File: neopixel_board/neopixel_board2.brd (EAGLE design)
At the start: 160 x 100 mm, 44 parts, among them J1 SSW-102-02-T-S-RA, J2 SSW-102-02-T-S-RA, J3 SSW-102-02-T-S-RA, J4 SSW-102-02-T-S-RA, U2 MIC5219, U3 ATMEGA32U4, Y1 16MHz

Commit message: board WIP traces started
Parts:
- added LD4, LD5, LD6: GREEN, SparkFun-LED:LED-0603
- added R10, R12, R9: 1kΩ, SparkFun:0603-RES
- moved R5 144.8 mm to (3.81, 3.81), turned to 90 degrees
- moved R4 134.9 mm to (12.7, 26.7)
- moved R7 134.7 mm to (7.62, 3.81), turned to 90 degrees
- moved D1 128.4 mm to (11.4, 3.81), turned to 90 degrees
- moved C13 120.9 mm to (38.1, 29.2)
- moved C19 113.7 mm to (38.1, 33.0)
- moved R2 112.1 mm to (49.5, 19.1), turned to 90 degrees
- moved R8 105.0 mm to (58.4, 7.62), turned to 90 degrees
- moved R3 104.0 mm to (34.3, 53.3), turned to 90 degrees
- moved C6 100.7 mm to (53.3, 7.62), turned to 90 degrees
- moved R6 100.6 mm to (49.5, 7.62), turned to 270 degrees
- moved C18 99.3 mm to (49.5, 30.5)
- moved C5 96.6 mm to (54.6, 22.9), turned to 90 degrees
- moved U2 94.8 mm to (44.5, 30.5)
- moved LD1 89.9 mm to (49.5, 2.54)
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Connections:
- new net N$14: LD4.A, R12.1
- new net N$15: LD5.A, R10.1
- new net N$16: LD6.A, R9.1
- net GND: now also LD4.C, LD5.C, LD6.C
- net N$10: now also R9.2
- net N$11: now also R10.2
- net N$12: now also R12.2
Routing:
- net GND: track 0.00 -> 338.9 mm, vias 0 -> 1
- net VCC1_3.3V: track 0.00 -> 130.7 mm, vias 0 -> 7
- net RAW: track 0.00 -> 93.3 mm
- net VCC_5V: track 0.00 -> 58.0 mm
- net ETH_RST: track 0.00 -> 56.8 mm, vias 0 -> 3
- net MCU_RST: track 0.00 -> 56.4 mm, vias 0 -> 3
- net D+: track 0.00 -> 41.7 mm
- net N$4: track 0.00 -> 34.1 mm, vias 0 -> 2
- net TXLED: track 0.00 -> 24.0 mm, vias 0 -> 2
- net ETH_SCNN: track 0.00 -> 22.9 mm, vias 0 -> 2
- net NEOPIXEL_0: track 0.00 -> 20.6 mm, vias 0 -> 2
- net N$3: track 0.00 -> 18.0 mm
- net N$12: track 0.00 -> 17.2 mm
- net N$11: track 0.00 -> 17.1 mm
- net N$10: track 0.00 -> 17.1 mm
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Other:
- board size 160 x 100 mm -> 60.9 x 75.9 mm

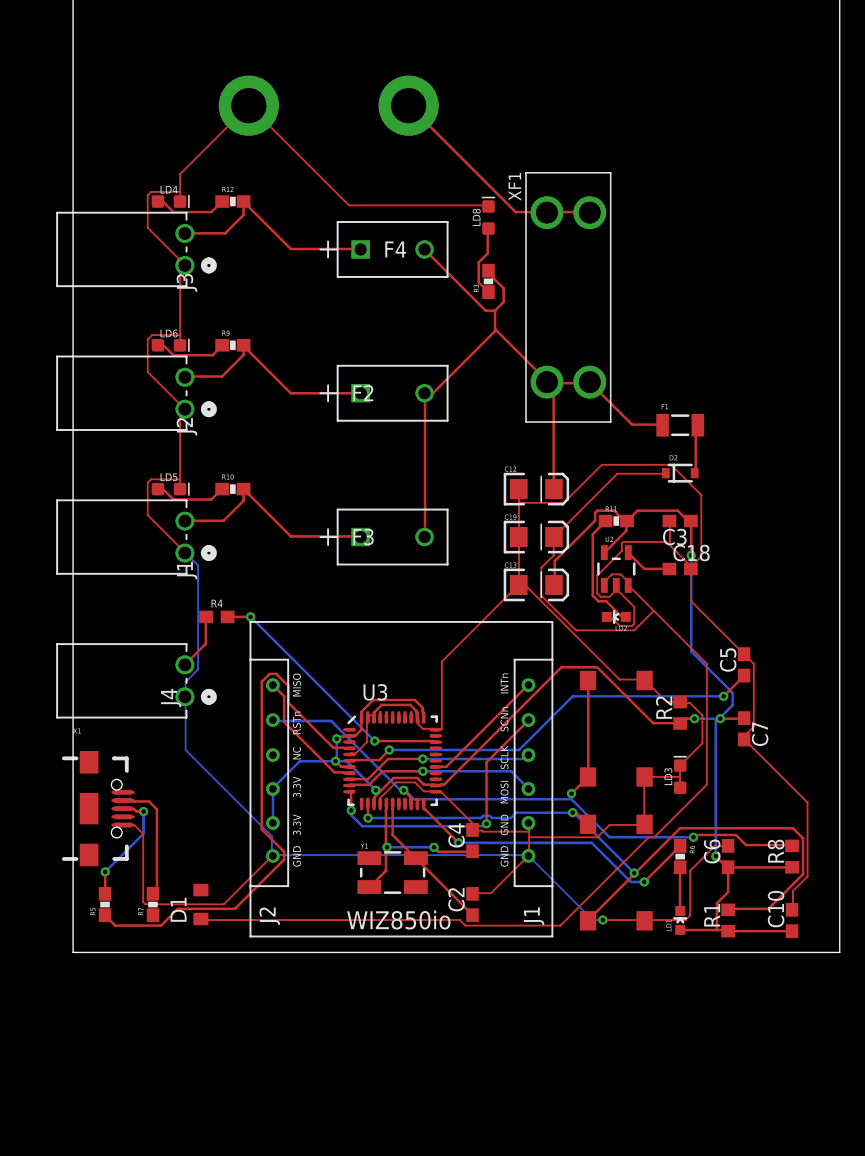
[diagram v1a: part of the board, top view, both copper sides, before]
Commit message: Schematic WIP
added new USB programmer, replaced fuse, ripup of autoroute
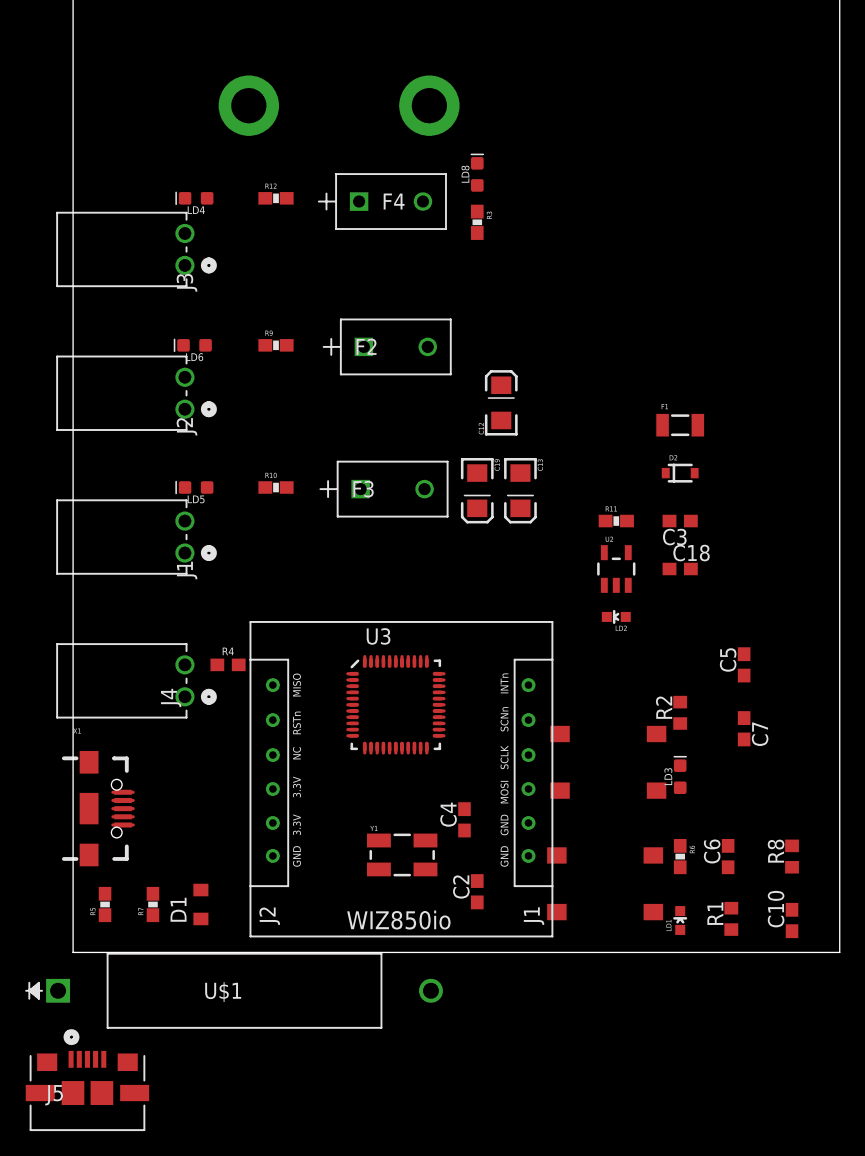
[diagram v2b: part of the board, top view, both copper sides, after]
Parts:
- removed XF1: 13A, RoboJackets-Fuses:3557-2
- added J5: 1981584-1, neopixel_board:CONN5_1981584-1
- added U$1: NEW_5STP, neopixel_board:5SP_AXIAL
- moved C13 7.60 mm to (36.8, 36.7), turned to 270 degrees
- moved C12 7.41 mm to (35.3, 43.7), turned to 90 degrees
- moved C19 5.97 mm to (33.4, 36.7), turned to 270 degrees
- moved R3 4.78 mm to (33.4, 58.0), turned to 270 degrees
- moved U3 4.45 mm to (26.9, 19.7)
- moved R4 3.91 mm to (13.6, 22.9)
- moved F4 3.81 mm to (29.1, 59.7)
- moved F3 3.81 mm to (29.2, 36.8)
- moved F2 3.69 mm to (29.5, 48.1)
- moved LD8 3.54 mm to (33.4, 61.8)
- moved R12 3.44 mm to (17.4, 59.9)
- moved R10 3.43 mm to (17.4, 37.0)
- moved R9 3.43 mm to (17.4, 48.3)
- moved PB2 2.74 mm to (43.8, 15.1), turned to 180 degrees
- moved LD4 2.17 mm to (11.0, 59.9), turned to 180 degrees
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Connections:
- net N$3: no longer XF1.1, XF1.2
- net VCC_5V: no longer XF1.3, XF1.4
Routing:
- net GND: track 338.9 -> 0.00 mm, vias 1 -> 0
- net VCC1_3.3V: track 130.7 -> 0.00 mm, vias 7 -> 0
- net RAW: track 93.3 -> 0.00 mm
- net VCC_5V: track 58.0 -> 0.00 mm
- net ETH_RST: track 56.8 -> 0.00 mm, vias 3 -> 0
- net MCU_RST: track 56.4 -> 0.00 mm, vias 3 -> 0
- net D+: track 41.7 -> 0.00 mm
- net N$4: track 34.1 -> 0.00 mm, vias 2 -> 0
- net TXLED: track 24.0 -> 0.00 mm, vias 2 -> 0
- net ETH_SCNN: track 22.9 -> 0.00 mm, vias 2 -> 0
- net NEOPIXEL_0: track 20.6 -> 0.00 mm, vias 2 -> 0
- net N$3: track 18.0 -> 0.00 mm
- net N$12: track 17.2 -> 0.00 mm
- net N$11: track 17.1 -> 0.00 mm
- net N$10: track 17.1 -> 0.00 mm
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
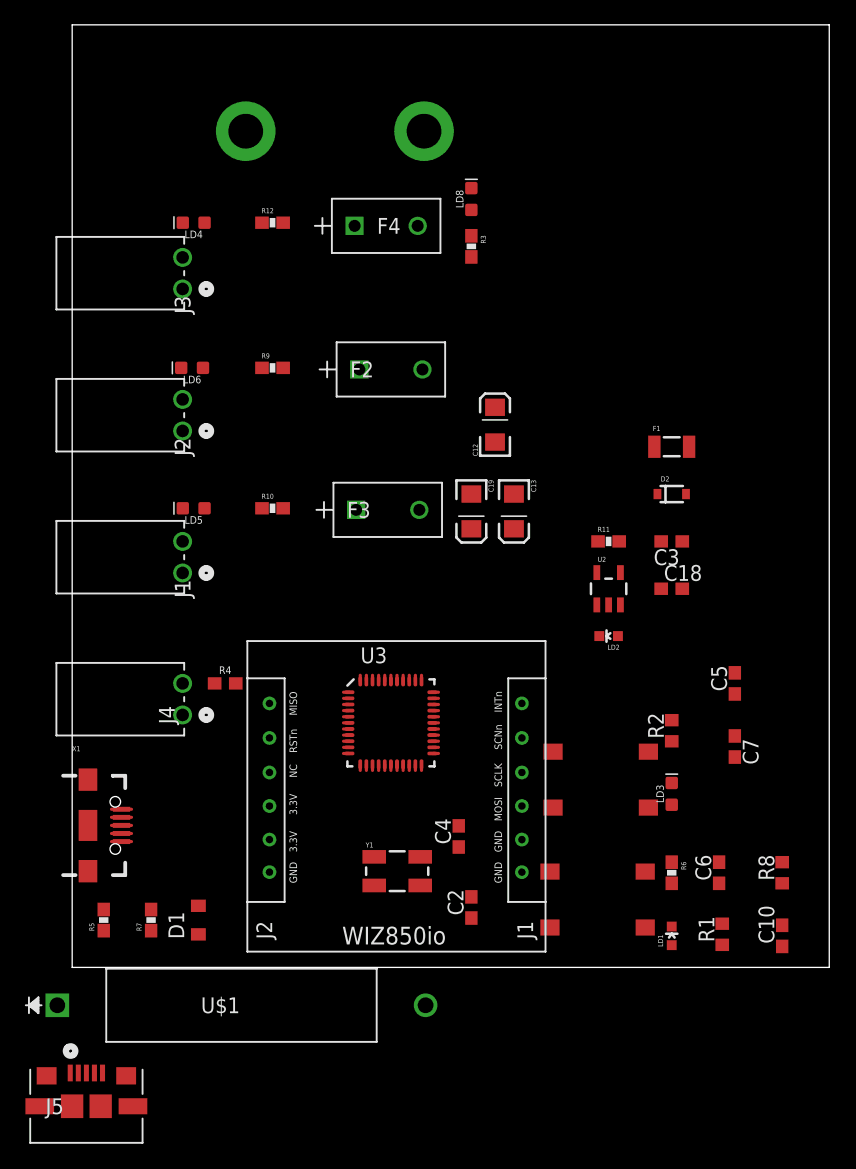
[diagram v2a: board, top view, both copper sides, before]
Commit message: Board, Schematic, Library WIP
Updated MCU, USB library layout of board completed, need to route
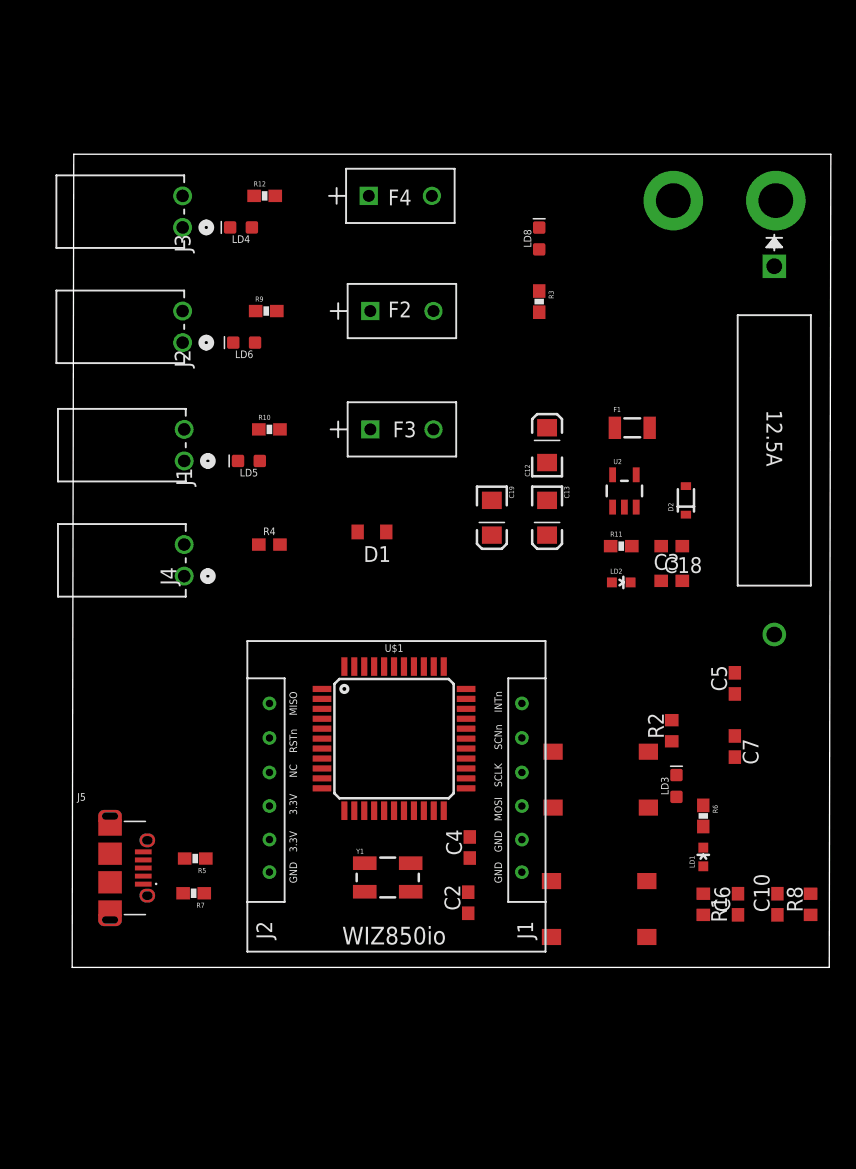
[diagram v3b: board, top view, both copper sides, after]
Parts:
- removed U3: ATMEGA32U4, Testing:QFN-44-NOPAD_1:1-OUTFAKES
- removed X1: (no value), Testing:USB-AB-MICRO-SMD-V03-IN&OUT
- added 12.5A: NEW_5STP, neopixel_board:5SP_AXIAL
- J5: value 1981584-1 -> 47589-0001; device neopixel_board:CONN5_1981584-1 -> 47589-0001:MOLEX_47589-0001
- U$1: value NEW_5STP -> 32U4; device neopixel_board:5SP_AXIAL -> SparkFun-IC-Microcontroller:TQFP44
- moved GND_TERMINAL 34.9 mm to (49.7, 61.7)
- moved D1 34.2 mm to (25.4, 35.1), turned to 180 degrees
- moved 5VSOURCE 28.9 mm to (57.9, 61.7)
- moved U$1 21.6 mm to (27.2, 18.4)
- moved J5 19.3 mm to (4.32, 8.00)
- moved R4 11.7 mm to (17.1, 34.0)
- moved J4 11.2 mm to (10.3, 32.8)
- moved J1 9.02 mm to (10.3, 42.0)
- moved R5 8.88 mm to (11.2, 8.76), turned to 180 degrees
- moved U2 7.98 mm to (45.7, 38.4)
- moved J2 7.11 mm to (10.2, 51.6)
- moved R3 7.04 mm to (38.9, 53.6)
- moved LD1 6.84 mm to (52.1, 8.89)
- moved F3 6.58 mm to (30.4, 43.3)
- moved R10 6.36 mm to (17.1, 43.3)
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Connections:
- removed net UVCC: D1.A, X1.VBUS1
- new net N$17: D1.A, J5.1
- new net N$18: LD3.A, R2.2
- net D+: now also U$1.4; no longer U3.4
- net D-: now also U$1.3; no longer U3.3
- net ETH_INT: now also U$1.27; no longer U3.27
- net ETH_MISO: now also U$1.8; no longer U3.8
- net ETH_MOSI: now also U$1.10; no longer U3.10
- net ETH_RST: now also U$1.20; no longer U3.20
- net ETH_SCK: now also U$1.9; no longer U3.9
- net ETH_SCNN: now also U$1.11; no longer U3.11
- net GND: now also J5.5, J5.P$1, J5.P$2, J5.P$3, J5.P$4, J5.P$5, J5.P$6, U$1.15, U$1.23, U$1.33, U$1.35, U$1.42, U$1.43, U$1.5; no longer LD3.A, R2.2, U3.15, U3.23, U3.33, U3.35, U3.42, U3.43, U3.5, X1.GND1
- net MCU_RST: now also U$1.13; no longer U3.13
- net N$1: now also U$1.16; no longer U3.16
- net N$2: now also U$1.17; no longer U3.17
- net N$3: now also 12.5A.1
- net N$4: now also U$1.6; no longer U3.6
- net N$6: now also J5.2; no longer X1.D-1
- net N$8: now also J5.3; no longer X1.D+1
- net NEOPIXEL_0: now also U$1.31; no longer U3.31
- net TXLED: now also U$1.22; no longer U3.22
- net VCC1_3.3V: now also U$1.14, U$1.2, U$1.24, U$1.34, U$1.44, U$1.7; no longer U3.14, U3.2, U3.24, U3.34, U3.44, U3.7
- net VCC_5V: now also 12.5A.2
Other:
- board size 60.9 x 75.9 mm -> 61.1 x 65.5 mm

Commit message: Board WIP
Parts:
- 12.5A: value NEW_5STP -> (none); device neopixel_board:5SP_AXIAL -> neopixel_board:3557-2
- F2, F3, F4: value RST_4-BULK -> (none); device neopixel_board:RST -> neopixel_board:3557-2
- moved 12.5A 26.8 mm to (49.9, 52.5)
- moved D1 21.1 mm to (43.9, 24.9)
- moved C12 18.2 mm to (57.4, 45.2)
- moved F1 12.9 mm to (57.1, 36.4)
- moved GND_TERMINAL 11.6 mm to (57.4, 53.1)
- moved LD5 9.78 mm to (5.71, 40.9)
- moved LD6 9.41 mm to (5.71, 50.7)
- moved R4 9.23 mm to (9.53, 28.8)
- moved LD4 9.20 mm to (5.71, 60.6)
- moved R10 7.99 mm to (9.53, 40.9)
- moved J4 7.88 mm to (9.91, 24.9)
- moved R9 7.68 mm to (9.53, 50.7)
- moved R12 7.40 mm to (9.53, 60.6)
- moved C13 5.51 mm to (40.3, 30.7)
- moved C19 5.36 mm to (33.8, 31.0)
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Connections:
- removed net N$3: 12.5A.1, 5VSOURCE.1
- new net 5VIN: 12.5A.1, 12.5A.2, 5VSOURCE.1
- net N$10: now also F2.2
- net N$11: now also F3.2
- net N$12: now also F4.2
- net VCC_5V: now also 12.5A.3, 12.5A.4, F2.3, F2.4, F3.3, F3.4, F4.3, F4.4; no longer 12.5A.2, F2.2, F3.2, F4.2
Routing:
- net N$12: track 0.00 -> 21.2 mm
- net N$10: track 0.00 -> 20.4 mm
- net N$11: track 0.00 -> 20.1 mm
- net GND: track 0.00 -> 19.4 mm, vias 0 -> 6
- net VCC_5V: track 0.00 -> 13.3 mm
- net N$21: track 0.00 -> 4.37 mm
- net N$13: track 0.00 -> 3.18 mm
- net N$16: track 0.00 -> 2.08 mm
- net N$15: track 0.00 -> 2.08 mm
- net N$14: track 0.00 -> 2.08 mm
- added copper zone on layer 1, net 5VIN
- added copper zone on layer 16, net GND
- added copper zone on layer 1, net VCC_5V
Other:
- outline, holes or cut-outs redrawn
